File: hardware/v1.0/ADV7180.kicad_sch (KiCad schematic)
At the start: 47 parts, among them J5 Conn_01x03, J6 Conn_01x03, J7 Conn_01x04, J8 Conn_01x34, U13 TLV75718PDRV, U2 CH32V003JxMx, U4 ADV7180BCP32Z-RL, U5 TLV62585, Y1 28.63636MHz

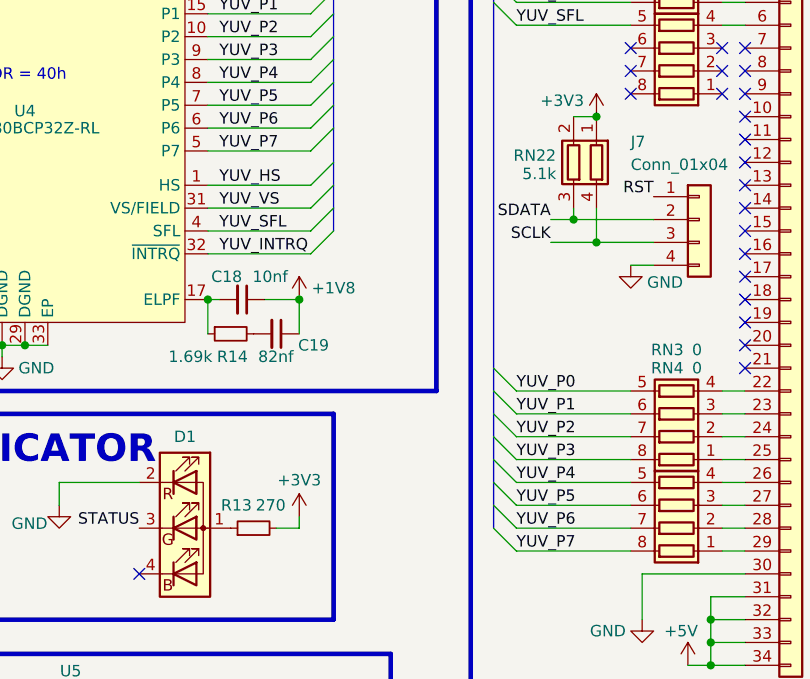
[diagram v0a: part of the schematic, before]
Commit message: did PORT0 routing
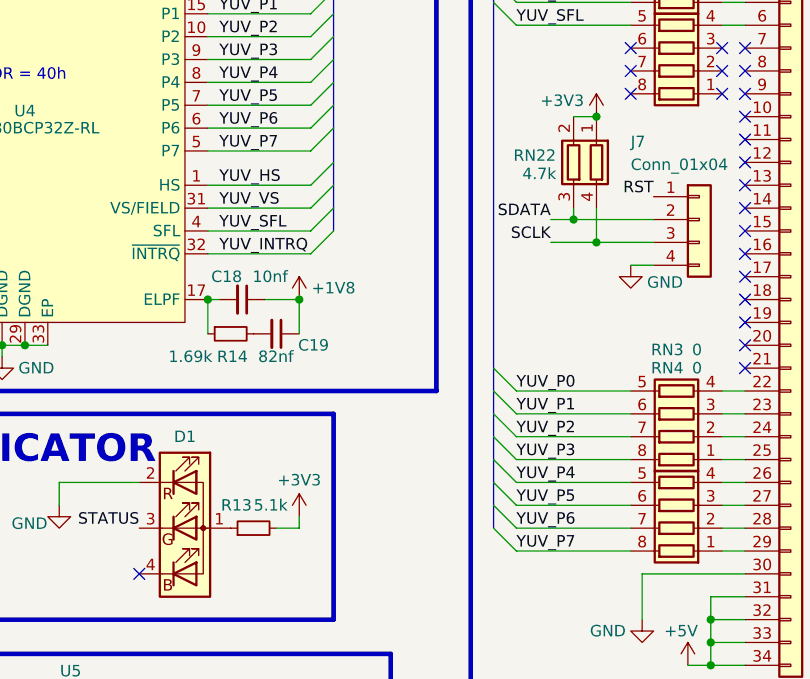
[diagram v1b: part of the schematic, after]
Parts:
- R13: value 270 -> 5.1k
- RN22: value 5.1k -> 4.7k; footprint (none) -> Resistor_SMD:R_Array_Convex_2x0603
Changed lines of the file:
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@@
 			)
 		)
-		(property "Value" "270"
+		(property "Value" "5.1k"
 			(at 103.505 96.52 90)
 			(effects
@@
 			)
 		)
-		(property "Value" "5.1k"
+		(property "Value" "4.7k"
 			(at 133.35 59.69 0)
 			(effects
@@
 			)
 		)
-		(property "Footprint" ""
+		(property "Footprint" "Resistor_SMD:R_Array_Convex_2x0603"
 			(at 132.715 58.42 90)
 			(effects

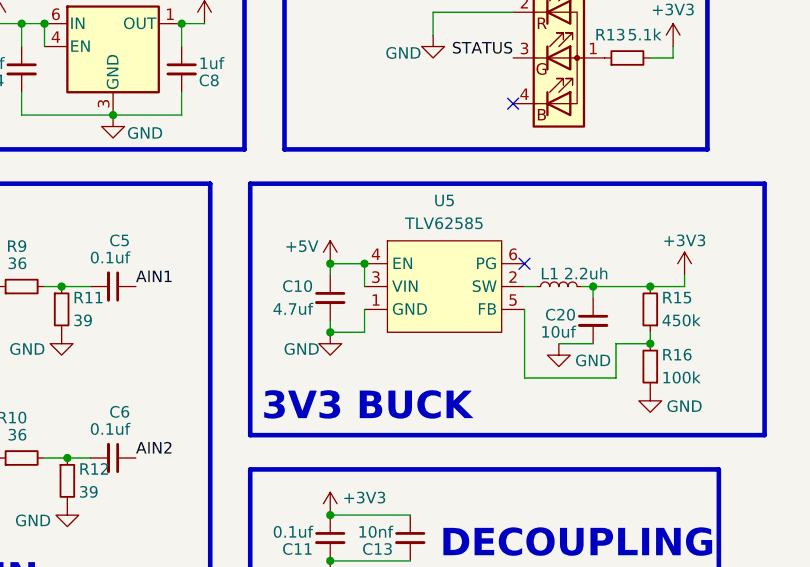
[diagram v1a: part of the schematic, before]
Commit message: redoing 3v3 regulators
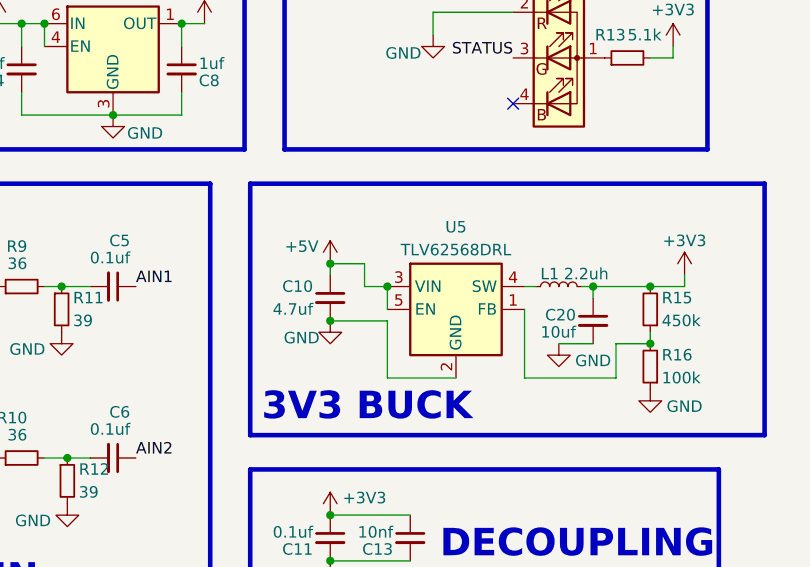
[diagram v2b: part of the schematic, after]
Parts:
- removed U5: TLV62585, Package_TO_SOT_SMD:SOT-563, symbol mylib:TLV62585
- added U5: TLV62568DRL, Package_TO_SOT_SMD:SOT-563, symbol Regulator_Switching:TLV62568DRL
- C10, C20: footprint Capacitor_SMD:C_0805_2012Metric -> Capacitor_SMD:C_0603_1608Metric
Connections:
- net +5V: now also U5.3 (VIN), U5.5 (EN)
- net GND: now also U5.2 (GND)
- net at R15.1, R16.2: now also U5.1 (FB)
- net at L1.1: now also U5.4 (SW)
- no-connect marks 24 -> 23
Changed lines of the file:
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@@
 	)
 	(junction
-		(at 68.58 129.54)
-		(diameter 0)
-		(color 0 0 0 0)
-	)
-	(junction
 		(at 38.735 124.46)
 		(diameter 0)
@@
 	)
 	(junction
-		(at 72.39 121.92)
+		(at 39.37 143.51)
 		(diameter 0)
 		(color 0 0 0 0)
 	)
 	(junction
-		(at 39.37 143.51)
+		(at 106.68 73.66)
 		(diameter 0)
 		(color 0 0 0 0)
 	)
 	(junction
-		(at 106.68 73.66)
+		(at 74.93 124.46)
 		(diameter 0)
 		(color 0 0 0 0)
@@
 	)
 	(junction
+		(at 68.58 128.27)
+		(diameter 0)
+		(color 0 0 0 0)
+	)
+	(junction
 		(at 76.2 78.74)
 		(diameter 0)
@@
 	)
 	(no_connect
-		(at 90.17 121.92)
-	)
-	(no_connect
 		(at 156.21 71.12)
 	)
@@
 	(wire
 		(pts
+			(xy 74.93 127) (xy 74.93 124.46)
+		)
+		(stroke
+			(width 0)
+			(type default)
+		)
+	)
+	(wire
+		(pts
 			(xy 137.16 53.34) (xy 139.7 53.34)
 		)
@@
 	(wire
 		(pts
-			(xy 77.47 162.56) (xy 86.36 162.56)
+			(xy 72.39 124.46) (xy 74.93 124.46)
 		)
 		(stroke
@@
 		)
 	)
-	(bus
+	(wire
 		(pts
-			(xy 128.27 91.44) (xy 128.27 93.98)
+			(xy 77.47 162.56) (xy 86.36 162.56)
 		)
 		(stroke
@@
 		)
 	)
-	(wire
+	(bus
 		(pts
-			(xy 130.81 88.9) (xy 143.51 88.9)
+			(xy 128.27 91.44) (xy 128.27 93.98)
 		)
 		(stroke
@@
 	(wire
 		(pts
-			(xy 97.79 124.46) (xy 104.14 124.46)
+			(xy 130.81 88.9) (xy 143.51 88.9)
 		)
 		(stroke
@@
 	(wire
 		(pts
-			(xy 48.26 69.85) (xy 54.61 69.85)
+			(xy 97.79 124.46) (xy 104.14 124.46)
 		)
 		(stroke
@@
 	(wire
 		(pts
-			(xy 52.07 95.25) (xy 52.07 97.79)
+			(xy 48.26 69.85) (xy 54.61 69.85)
 		)
 		(stroke
@@
 	(wire
 		(pts
-			(xy 72.39 127) (xy 72.39 129.54)
+			(xy 52.07 95.25) (xy 52.07 97.79)
 		)
 		(stroke
@@
 	(wire
 		(pts
-			(xy 76.2 78.74) (xy 73.66 78.74)
+			(xy 74.93 128.27) (xy 74.93 134.62)
 		)
 		(stroke
@@
 	(wire
 		(pts
-			(xy 68.58 129.54) (xy 72.39 129.54)
+			(xy 76.2 78.74) (xy 73.66 78.74)
 		)
 		(stroke
@@
 	(wire
 		(pts
-			(xy 68.58 129.54) (xy 68.58 128.27)
+			(xy 68.58 121.92) (xy 68.58 123.19)
 		)
 		(stroke
@@
 	(wire
 		(pts
-			(xy 68.58 121.92) (xy 68.58 123.19)
+			(xy 100.33 130.81) (xy 104.14 130.81)
 		)
 		(stroke
@@
 	(wire
 		(pts
-			(xy 100.33 130.81) (xy 104.14 130.81)
+			(xy 152.4 111.76) (xy 156.21 111.76)
 		)
 		(stroke
@@
 		)
 	)
-	(wire
+	(bus
 		(pts
-			(xy 152.4 111.76) (xy 156.21 111.76)
+			(xy 110.49 49.53) (xy 110.49 52.07)
 		)
 		(stroke
@@
 		)
 	)
-	(bus
+	(wire
 		(pts
-			(xy 110.49 49.53) (xy 110.49 52.07)
+			(xy 130.81 101.6) (xy 143.51 101.6)
 		)
 		(stroke
@@
 	(wire
 		(pts
-			(xy 130.81 101.6) (xy 143.51 101.6)
+			(xy 68.58 128.27) (xy 74.93 128.27)
 		)
 		(stroke
@@
 	(wire
 		(pts
+			(xy 74.93 134.62) (xy 82.55 134.62)
+		)
+		(stroke
+			(width 0)
+			(type default)
+		)
+	)
+	(wire
+		(pts
 			(xy 153.67 43.18) (xy 156.21 43.18)
 		)
@@
 			)
 		)
-		(property "Footprint" "Capacitor_SMD:C_0805_2012Metric"
+		(property "Footprint" "Capacitor_SMD:C_0603_1608Metric"
 			(at 68.58 125.73 0)
 			(effects
@@
 	(symbol
 		(lib_id "power:GND")
-		(at 68.58 129.54 0)
+		(at 68.58 128.27 0)
 		(unit 1)
 		(exclude_from_sim no)
@@
 		(dnp no)
 		(property "Reference" "#PWR30"
-			(at 68.58 135.89 0)
+			(at 68.58 134.62 0)
 			(effects
 				(font
@@
 		)
 		(property "Value" "GND"
-			(at 65.405 131.445 0)
+			(at 65.405 130.175 0)
 			(effects
 				(font
@@
 		)
 		(property "Footprint" ""
-			(at 68.58 129.54 0)
+			(at 68.58 128.27 0)
 			(effects
 				(font
@@
 		)
 		(property "Datasheet" ""
-			(at 68.58 129.54 0)
+			(at 68.58 128.27 0)
 			(effects
 				(font
@@
 		)
 		(property "Description" "Power symbol creates a global label with name \"GND\" , ground"
-			(at 68.58 129.54 0)
+			(at 68.58 128.27 0)
 			(effects
 				(font
@@
 	)
 	(symbol
+		(lib_id "Regulator_Switching:TLV62568DRL")
+		(at 82.55 127 0)
+		(unit 1)
+		(exclude_from_sim no)
+		(in_bom yes)
+		(on_board yes)
+		(dnp no)
+		(property "Reference" "U5"
+			(at 82.55 117.856 0)
+			(effects
+				(font
+					(size 1.27 1.27)
+				)
+			)
+		)
+		(property "Value" "TLV62568DRL"
+			(at 82.55 120.396 0)
+			(effects
+				(font
+					(size 1.27 1.27)
+				)
+			)
+		)
+		(property "Footprint" "Package_TO_SOT_SMD:SOT-563"
+			(at 83.82 133.35 0)
+			(effects
+				(font
+					(size 1.27 1.27)
+					(italic yes)
+				)
+				(justify left)
+				(hide yes)
+			)
+		)
+		(property "Datasheet" "http://www.ti.com/lit/ds/symlink/tlv62568.pdf"
+			(at 76.2 115.57 0)
+			(effects
+				(font
+					(size 1.27 1.27)
+				)
+				(hide yes)
+			)
+		)
+		(property "Description" "High Efficiency Synchronous Buck Converter, Adjustable Output 0.6V-5.5V, 1A, SOT-563-6"
+			(at 82.55 127 0)
+			(effects
+				(font
+					(size 1.27 1.27)
+				)
+				(hide yes)
+			)
+		)
+		(pin "3"
+		)
+		(pin "5"
+		)
+		(pin "1"
+		)
+		(pin "4"
+		)
+		(pin "6"
+		)
+		(pin "2"
+		)
+		(instances
+			(project ""
+				(path "/1a66a179-6cc4-4048-836e-3eb434e9da88/856c4711-f246-4385-ad64-862f60e59bf4"
+					(reference "U5")
+					(unit 1)
+				)
+			)
+		)
+	)
+	(symbol
 		(lib_id "Device:R_Small")
 		(at 34.29 124.46 90)
@@
 			)
 		)
-		(property "Footprint" "Capacitor_SMD:C_0805_2012Metric"
+		(property "Footprint" "Capacitor_SMD:C_0603_1608Metric"
 			(at 97.79 128.27 0)
 			(effects
@@
 					(unit 1)
 				)
-			)
-		)
-	)
-	(symbol
-		(lib_id "mylib:TLV62585")
-		(at 81.28 124.46 0)
-		(unit 1)
-		(exclude_from_sim no)
-		(in_bom yes)
-		(on_board yes)
-		(dnp no)
-		(fields_autoplaced yes)
-		(property "Reference" "U5"
-			(at 81.28 114.935 0)
-			(effects
-				(font
-					(size 1.27 1.27)
-				)
-			)
-		)
-		(property "Value" "TLV62585"
-			(at 81.28 117.475 0)
-			(effects
-				(font
-					(size 1.27 1.27)
-				)
-			)
-		)
-		(property "Footprint" "Package_TO_SOT_SMD:SOT-563"
-			(at 81.28 124.46 0)
-			(effects
-				(font
-					(size 1.27 1.27)
-				)
-				(hide yes)
-			)
-		)
-		(property "Datasheet" ""
-			(at 81.28 124.46 0)
-			(effects
-				(font
-					(size 1.27 1.27)
-				)
-				(hide yes)
-			)
-		)
-		(property "Description" ""
-			(at 81.28 124.46 0)
-			(effects
-				(font
-					(size 1.27 1.27)
-				)
-				(hide yes)
-			)
-		)
-		(pin "5"
-		)
-		(pin "1"
-		)
-		(pin "6"
-		)
-		(pin "3"
-		)
-		(pin "2"
-		)
-		(pin "4"
-		)
-		(instances
-			(project "QMTECH_XC7A100T-Expantion-Board"
-				(path "/1a66a179-6cc4-4048-836e-3eb434e9da88/856c4711-f246-4385-ad64-862f60e59bf4"
-					(reference "U5")
-					(unit 1)
-				)

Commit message: finished first draft, still DRC errors
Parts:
- removed U4: ADV7180BCP32Z-RL, Package_CSP:LFCSP-32-1EP_5x5mm_P0.5mm_EP3.6x3.6mm, symbol C459884:ADV7180BCP32Z-RL
- added U4: ADV7180BCP32Z-RL, C459884:LFCSP-32_L5.0-W5.0-P0.50-BL-EP3.6, symbol adv7180:ADV7180BCP32Z-RL
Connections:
- net +1V8: now also U4.14 (DVDD), U4.18 (PVDD), U4.22 (AVDD), U4.30 (DVDD)
- net +3V3: now also U4.3 (DVDDIO)
- net AIN1: now also U4.23 (AIN1)
- net AIN2: now also U4.19 (AIN2)
- net ALSB: now also U4.26 (ALSB)
- net GND: now also U4.2 (DGND), U4.29 (DGND), U4.33 (EP)
- net RST: now also U4.25 (~{RESET})
- net SCLK: now also U4.28 (SCLK)
- net SDATA: now also U4.27 (SDATA)
- net YUV_CLK: now also U4.11 (LLC)
- net YUV_HS: now also U4.1 (HS)
- net YUV_INTRQ: now also U4.32 (~{INTRQ})
- net YUV_P0: now also U4.16 (P0)
- net YUV_P1: now also U4.15 (P1)
- net YUV_P2: now also U4.10 (P2)
- net YUV_P3: now also U4.9 (P3)
- net YUV_P4: now also U4.8 (P4)
- net YUV_P5: now also U4.7 (P5)
- net YUV_P6: now also U4.6 (P6)
- net YUV_P7: now also U4.5 (P7)
- net YUV_SFL: now also U4.4 (SFL)
- net YUV_VS: now also U4.31 (VS/FIELD)
- net at C2.1, Y1.1: now also U4.12 (XTAL1)
- net at C3.1, Y1.3: now also U4.13 (XTAL)
- net at C18.2, R14.1: now also U4.17 (ELPF)
- net at C7.2: now also U4.20 (VREFP)
- net at C7.1: now also U4.21 (VREFN)
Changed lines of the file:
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@@
 	)
 	(junction
+		(at 76.2 78.74)
+		(diameter 0)
+		(color 0 0 0 0)
+	)
+	(junction
 		(at 38.735 124.46)
 		(diameter 0)
@@
 	)
 	(junction
+		(at 96.52 73.66)
+		(diameter 0)
+		(color 0 0 0 0)
+	)
+	(junction
 		(at 77.47 162.56)
 		(diameter 0)
@@
 	)
 	(junction
-		(at 96.52 73.66)
-		(diameter 0)
-		(color 0 0 0 0)
-	)
-	(junction
 		(at 77.47 167.64)
 		(diameter 0)
@@
 	)
 	(junction
-		(at 76.2 30.48)
-		(diameter 0)
-		(color 0 0 0 0)
-	)
-	(junction
 		(at 68.58 167.64)
 		(diameter 0)
@@
 	)
 	(junction
-		(at 76.2 78.74)
-		(diameter 0)
-		(color 0 0 0 0)
-	)
-	(junction
 		(at 152.4 109.22)
 		(diameter 0)
@@
 	)
 	(junction
-		(at 73.66 78.74)
-		(diameter 0)
-		(color 0 0 0 0)
-	)
-	(junction
 		(at 139.7 67.31)
 		(diameter 0)
@@
 	)
 	(junction
-		(at 85.09 30.48)
+		(at 76.2 30.48)
 		(diameter 0)
 		(color 0 0 0 0)
@@
 	)
 	(junction
+		(at 73.66 78.74)
+		(diameter 0)
+		(color 0 0 0 0)
+	)
+	(junction
 		(at 36.83 95.25)
 		(diameter 0)
@@
 		(color 0 0 0 0)
 	)
+	(junction
+		(at 85.09 30.48)
+		(diameter 0)
+		(color 0 0 0 0)
+	)
 	(no_connect
 		(at 143.51 50.8)
@@
 	)
 	(no_connect
-		(at 54.61 40.64)
-	)
-	(no_connect
 		(at 156.21 71.12)
 	)
@@
 	)
 	(no_connect
+		(at 54.61 40.64)
+	)
+	(no_connect
 		(at 156.21 73.66)
 	)
@@
 	(wire
 		(pts
-			(xy 78.74 78.74) (xy 76.2 78.74)
+			(xy 73.66 78.74) (xy 76.2 78.74)
 		)
 		(stroke
@@
 	(wire
 		(pts
-			(xy 76.2 78.74) (xy 73.66 78.74)
-		)
-		(stroke
-			(width 0)
-			(type default)
-		)
-	)
-	(wire
-		(pts
 			(xy 44.45 74.93) (xy 44.45 76.2)
 		)
@@
 		)
 	)
+	(wire
+		(pts
+			(xy 76.2 78.74) (xy 78.74 78.74)
+		)
+		(stroke
+			(width 0)
+			(type default)
+		)
+	)
 	(bus
 		(pts
@@
 	)
 	(symbol
-		(lib_id "C459884:ADV7180BCP32Z-RL")
-		(at 76.2 55.88 0)
-		(unit 1)
-		(exclude_from_sim no)
-		(in_bom yes)
-		(on_board yes)
-		(dnp no)
-		(property "Reference" "U4"
-			(at 76.2 52.705 0)
-			(effects
-				(font
-					(size 1.27 1.27)
-				)
-			)
-		)
-		(property "Value" "ADV7180BCP32Z-RL"
-			(at 75.565 54.61 0)
-			(effects
-				(font
-					(size 1.27 1.27)
-				)
-			)
-		)
-		(property "Footprint" "Package_CSP:LFCSP-32-1EP_5x5mm_P0.5mm_EP3.6x3.6mm"
-			(at 76.2 83.82 0)
-			(effects
-				(font
-					(size 1.27 1.27)
-				)
-				(hide yes)
-			)
-		)
-		(property "Datasheet" "https://lcsc.com/product-detail/Video-Audio-Interface-ICs_Analog-Devices-ADI-LINEAR-ADV7180BCP32Z-RL_C459884.html"
-			(at 76.2 86.36 0)
-			(effects
-				(font
-					(size 1.27 1.27)
-				)
-				(hide yes)
-			)
-		)
-		(property "Description" ""
-			(at 76.2 55.88 0)
-			(effects
-				(font
-					(size 1.27 1.27)
-				)
-				(hide yes)
-			)
-		)
-		(property "LCSC Part" "C459884"
-			(at 76.2 88.9 0)
-			(effects
-				(font
-					(size 1.27 1.27)
-				)
-				(hide yes)
-			)
-		)
-		(pin "1"
-		)
-		(pin "10"
-		)
-		(pin "11"
-		)
-		(pin "12"
-		)
-		(pin "13"
-		)
-		(pin "14"
-		)
-		(pin "15"
-		)
-		(pin "16"
-		)
-		(pin "17"
-		)
-		(pin "18"
-		)
-		(pin "2"
-		)
-		(pin "20"
-		)
-		(pin "21"
-		)
-		(pin "22"
-		)
-		(pin "25"
-		)
-		(pin "26"
-		)
-		(pin "27"
-		)
-		(pin "28"
-		)
-		(pin "29"
-		)
-		(pin "3"
-		)
-		(pin "30"
-		)
-		(pin "31"
-		)
-		(pin "32"
-		)
-		(pin "33"
-		)
-		(pin "4"
-		)
-		(pin "5"
-		)
-		(pin "6"
-		)
-		(pin "7"
-		)
-		(pin "8"
-		)
-		(pin "9"
-		)
-		(pin "23"
-		)
-		(pin "19"
-		)
-		(pin "30"
-		)
-		(instances
-			(project "QMTECH_XC7A100T-Expantion-Board"
-				(path "/1a66a179-6cc4-4048-836e-3eb434e9da88/856c4711-f246-4385-ad64-862f60e59bf4"
-					(reference "U4")
-					(unit 1)
-				)
-			)
-		)
-	)
-	(symbol
 		(lib_id "Device:C_Small")
 		(at 177.8 27.94 0)
@@
 					(unit 1)
 				)
+			)
+		)
+	)
+	(symbol
+		(lib_id "adv7180:ADV7180BCP32Z-RL")
+		(at 76.2 55.88 0)
+		(unit 1)
+		(exclude_from_sim no)
+		(in_bom yes)
+		(on_board yes)
+		(dnp no)
+		(fields_autoplaced yes)
+		(property "Reference" "U4"
+			(at 80.8833 78.74 0)
+			(effects
+				(font
+					(size 1.27 1.27)
+				)
+				(justify left)
+			)
+		)
+		(property "Value" "ADV7180BCP32Z-RL"
+			(at 80.8833 81.28 0)
+			(effects
+				(font
+					(size 1.27 1.27)
+				)
+				(justify left)
+			)
+		)
+		(property "Footprint" "C459884:LFCSP-32_L5.0-W5.0-P0.50-BL-EP3.6"
+			(at 83.82 83.82 0)
+			(effects
+				(font
+					(size 1.27 1.27)
+				)
+				(hide yes)
+			)
+		)
+		(property "Datasheet" "https://lcsc.com/product-detail/Video-Audio-Interface-ICs_Analog-Devices-ADI-LINEAR-ADV7180BCP32Z-RL_C459884.html"
+			(at 76.2 86.36 0)
+			(effects
+				(font
+					(size 1.27 1.27)
+				)
+				(hide yes)
+			)
+		)
+		(property "Description" ""
+			(at 76.2 55.88 0)
+			(effects
+				(font
+					(size 1.27 1.27)
+				)
+				(hide yes)
+			)
+		)
+		(property "LCSC Part" "C459884"
+			(at 81.28 88.9 0)
+			(effects
+				(font
+					(size 1.27 1.27)
+				)
+				(hide yes)
+			)
+		)
+		(pin "33"
+		)
+		(pin "14"
+		)
+		(pin "11"
+		)
+		(pin "19"
+		)
+		(pin "5"
+		)
+		(pin "2"
+		)
+		(pin "26"
+		)
+		(pin "20"
+		)
+		(pin "4"
+		)
+		(pin "27"
+		)
+		(pin "31"
+		)
+		(pin "16"
+		)
+		(pin "21"
+		)
+		(pin "22"
+		)
+		(pin "18"
+		)
+		(pin "23"
+		)
+		(pin "3"
+		)
+		(pin "1"
+		)
+		(pin "17"
+		)
+		(pin "8"
+		)
+		(pin "25"
+		)
+		(pin "13"
+		)
+		(pin "12"
+		)
+		(pin "10"
+		)
+		(pin "9"
+		)
+		(pin "29"
+		)
+		(pin "7"
+		)
+		(pin "32"
+		)
+		(pin "30"
+		)
+		(pin "24"
+		)
+		(pin "15"
+		)
+		(pin "28"
+		)
+		(pin "6"
+		)
+		(instances
+			(project ""
+				(path "/1a66a179-6cc4-4048-836e-3eb434e9da88/856c4711-f246-4385-ad64-862f60e59bf4"
+					(reference "U4")
+					(unit 1)
+				)
